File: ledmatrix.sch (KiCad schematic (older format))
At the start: 23 parts, among them U2 IS31FL3737, U3 IS31FL3737

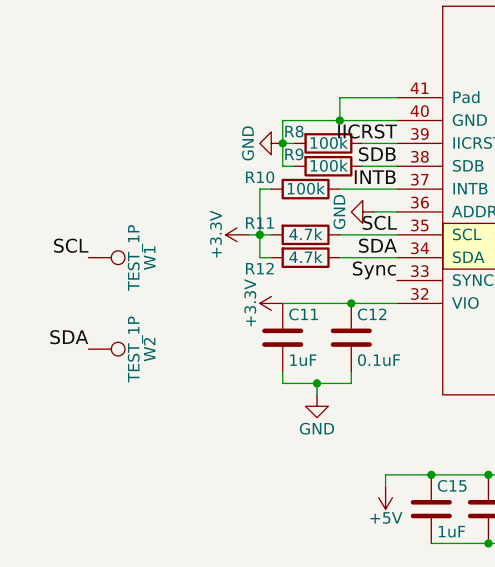
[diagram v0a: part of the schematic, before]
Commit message: Switched to different Debug Ports
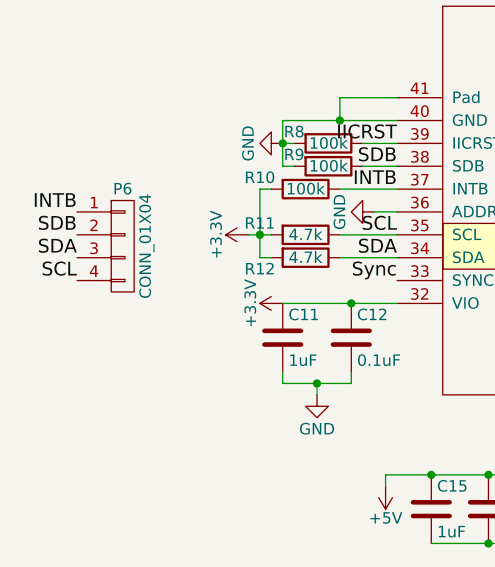
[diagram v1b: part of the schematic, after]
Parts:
- removed W1, W2: TEST_1P, Measurement_Points:Measurement_Point_Round-SMD-Pad_Small, symbol TEST_1P
- added P6: CONN_01X04, lib.pretty:Conn-4, symbol CONN_01X04
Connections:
- net INTB: now also P6.1 (P1)
- net SCL: now also P6.4 (P4)
- net SDA: now also P6.3 (P3)
- net SDB: now also P6.2 (P2)
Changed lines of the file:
@@
 Text Label 2700 1450 0    60   ~ 0
 SDA
-Text Label 1650 2950 2    60   ~ 0
-SCL
-Text Label 1650 3350 2    60   ~ 0
-SDA
-$Comp
-L TEST_1P W1
-U 1 1 5766B03E
-P 1650 2950
-F 0 "W1" H 1650 3220 50  0000 C CNN
-F 1 "TEST_1P" H 1650 3150 50  0000 C CNN
-F 2 "Measurement_Points:Measurement_Point_Round-SMD-Pad_Small" H 1850 2950 50  0001 C CNN
-F 3 "" H 1850 2950 50  0000 C CNN
-	1    1650 2950
-	0    1    1    0
-$EndComp
-$Comp
-L TEST_1P W2
-U 1 1 5766B419
-P 1650 3350
-F 0 "W2" H 1650 3620 50  0000 C CNN
-F 1 "TEST_1P" H 1650 3550 50  0000 C CNN
-F 2 "Measurement_Points:Measurement_Point_Round-SMD-Pad_Small" H 1850 3350 50  0001 C CNN
-F 3 "" H 1850 3350 50  0000 C CNN
-	1    1650 3350
-	0    1    1    0
-$EndComp
 Wire Wire Line
 	6600 2350 6750 2350
@@
 	2450 2650 2400 2650
 Connection ~ 2400 2850
+$Comp
+L CONN_01X04 P6
+U 1 1 578A6B55
+P 1800 2900
+F 0 "P6" H 1800 3150 50  0000 C CNN
+F 1 "CONN_01X04" V 1900 2900 50  0000 C CNN
+F 2 "lib.pretty:Conn-4" H 1800 2900 50  0001 C CNN
+F 3 "" H 1800 2900 50  0000 C CNN
+	1    1800 2900
+	1    0    0    -1
+$EndComp
+Text Label 1600 2750 2    60   ~ 0
+INTB
+Text Label 1600 2850 2    60   ~ 0
+SDB
+Text Label 1600 3050 2    60   ~ 0
+SCL
+Text Label 1600 2950 2    60   ~ 0
+SDA
 $EndSCHEMATC
